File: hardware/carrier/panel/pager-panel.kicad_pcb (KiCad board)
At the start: 2 copper layers, 40 x 20 mm, 28 parts, among them J1 GDEY029T94 FPC, J2 CARRIER, J3 FL-A FPC (FL03), J4 FL-B FPC (Orient), Q5 AO3400A

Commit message: BOM: move six passives to JLC basic parts, fix connector LCSC codes (no footprint changes)
Carrier: R32 2.2M -> 1M (C26083), C14 22nF -> 100nF (C1525), R1 22.1k -> 22k (C25768),
R2 47.5k -> 47k (C25792); J1 LCSC C160407 (SM08B), J2 MPN/LCSC SM04B-SRSS-TB C160404
to match its SH footprint.
Panel: C11 4.7uF under basic code C19666, D1-D3 NSR0530 -> B5819W (C8598, SOD-123 as
already on the board), R4 2.2R gets C22939.
Board footprint fields updated to match. ERC clean on both.

Co-Authored-By: Claude Fable 5.1 <noreply@anthropic.com>
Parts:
- D1, D2, D3: value MBR0530 -> B5819W
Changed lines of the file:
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@@
 			)
 		)
-		(property "LCSC" "C1779"
+		(property "LCSC" "C19666"
 			(at 0 0 90)
 			(layer "F.Fab")
@@
 			)
 		)
-		(property "Value" "MBR0530"
+		(property "Value" "B5819W"
 			(at 0 2.1 0)
 			(layer "F.Fab")
@@
 			)
 		)
-		(property "MPN" "MBR0530"
+		(property "MPN" "B5819W"
 			(at 0 0 0)
 			(layer "F.Fab")
@@
 			)
 		)
-		(property "LCSC" "C82046"
+		(property "LCSC" "C8598"
 			(at 0 0 0)
 			(layer "F.Fab")
@@
 			)
 		)
-		(property "Value" "MBR0530"
+		(property "Value" "B5819W"
 			(at 0 2.1 0)
 			(layer "F.Fab")
@@
 			)
 		)
-		(property "MPN" "MBR0530"
+		(property "MPN" "B5819W"
 			(at 0 0 0)
 			(layer "F.Fab")
@@
 			)
 		)
-		(property "LCSC" "C82046"
+		(property "LCSC" "C8598"
 			(at 0 0 0)
 			(layer "F.Fab")
@@
 			)
 		)
-		(property "Value" "MBR0530"
+		(property "Value" "B5819W"
 			(at 0 2.1 0)
 			(layer "F.Fab")
@@
 			)
 		)
-		(property "MPN" "MBR0530"
+		(property "MPN" "B5819W"
 			(at 0 0 0)
 			(layer "F.Fab")
@@
 			)
 		)
-		(property "LCSC" "C82046"
+		(property "LCSC" "C8598"
 			(at 0 0 0)
 			(layer "F.Fab")
@@
 			)
 		)
-		(property "LCSC" ""
+		(property "LCSC" "C22939"
 			(at 0 0 90)
 			(layer "F.Fab")

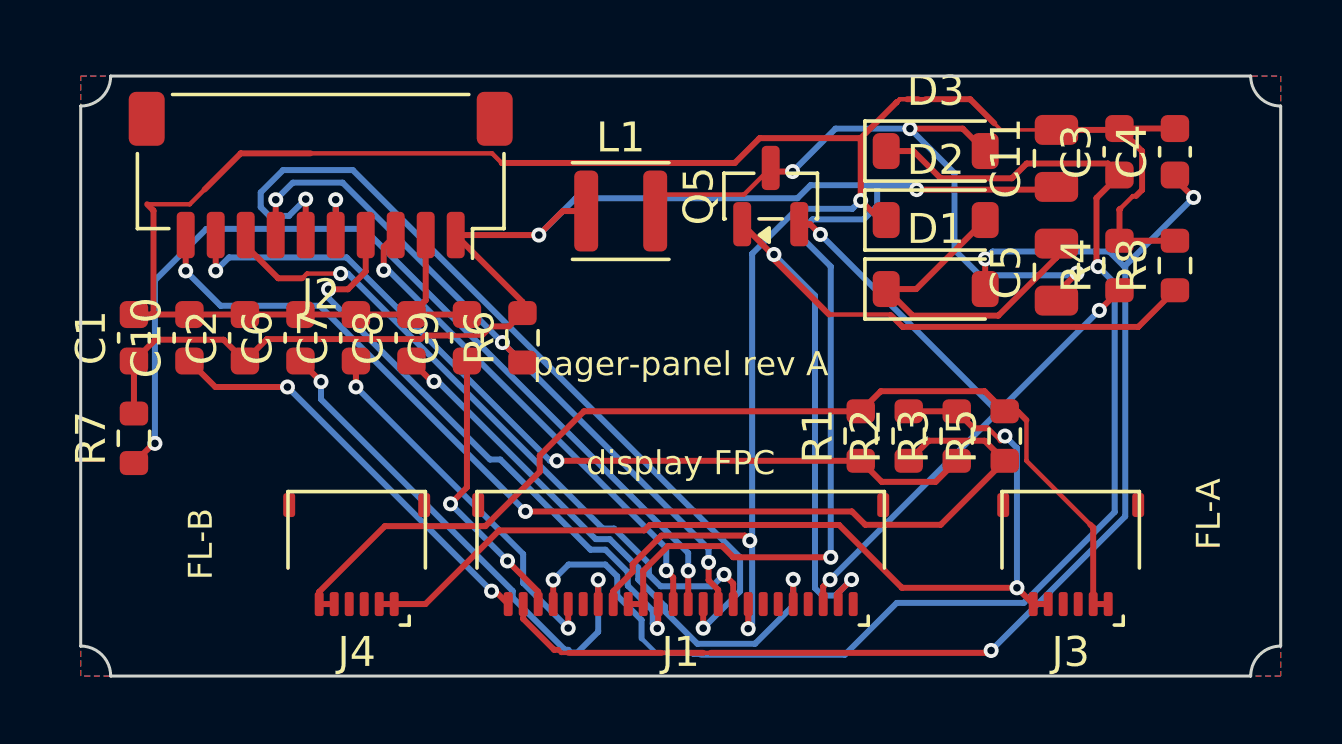
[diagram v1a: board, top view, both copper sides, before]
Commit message: Panel: split the frontlight off the carrier cable (J2 -> 8-pin SH, new J5 2-pin), re-routed
Schematic: J2 CARRIER is SM08B-SRSS-TB (C160407) on the same wires; new J5 FRONTLIGHT
SM02B-SRSS-TB (C160402) takes FL_P (pin 1) and FL_N (pin 2), matching carrier J8.
Board: J2 swapped with pins 1-8 in place, J5 at the bottom-left corner, R7 nudged,
full Freerouting pass (0 unrouted), GND pours refilled.
Known: 25 tracks below the 0.2 mm minimum width, J5 mounting pads 0.2 mm too close to
the bottom edge; owner finishing by hand.

Co-Authored-By: Claude Fable 5.1 <noreply@anthropic.com>
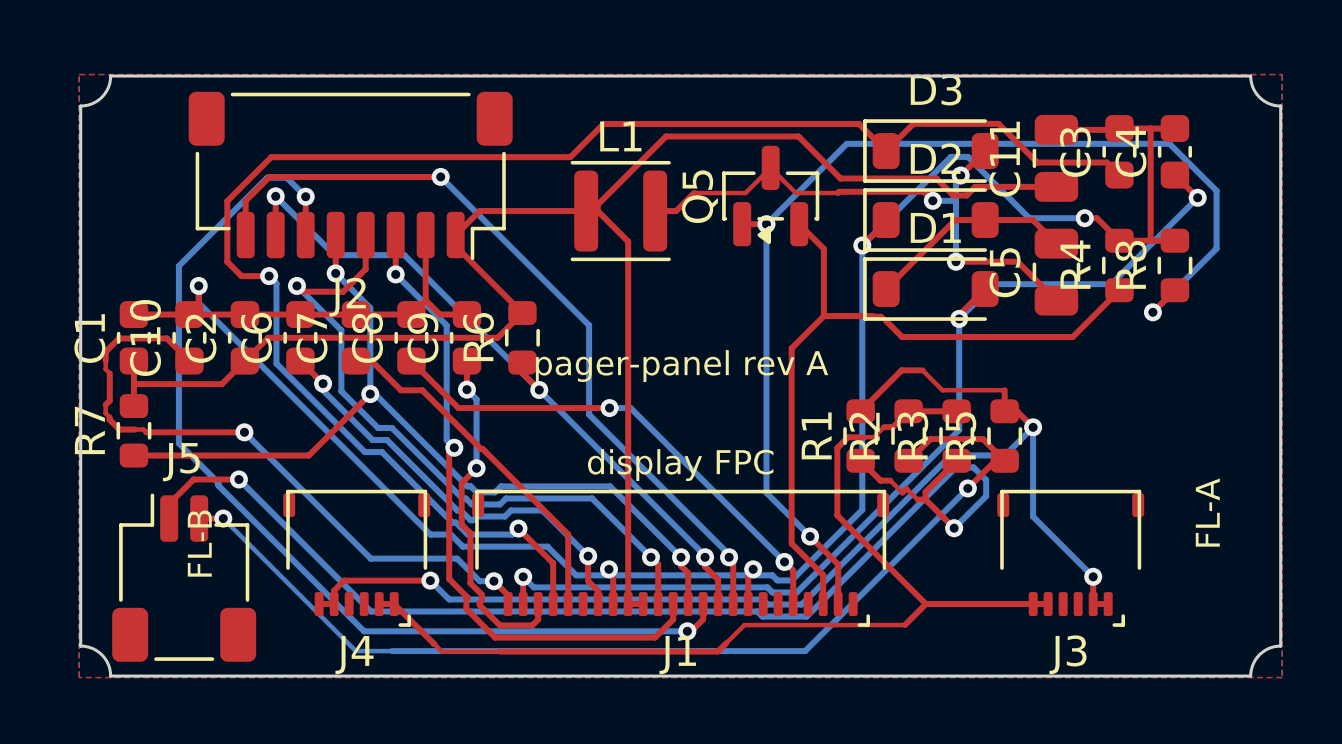
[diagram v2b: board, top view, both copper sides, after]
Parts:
- added J5: FRONTLIGHT, Connector_JST:JST_SH_SM02B-SRSS-TB_1x02-1MP_P1.00mm_Horizontal, F.Cu at (3.45, 16.8)
- J2: footprint Connector_JST:JST_SH_SM10B-SRSS-TB_1x10-1MP_P1.00mm_Horizontal -> Connector_JST:JST_SH_SM08B-SRSS-TB_1x08-1MP_P1.00mm_Horizontal
- moved J2 1.00 mm to (9.00, 3.30)
- moved R7 0.25 mm to (1.77, 11.8)
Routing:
- net GND: track 87.4 -> 75.6 mm, vias 3 -> 5
- net FL_P: track 29.5 -> 40.1 mm
- net 3V3_EPD: track 65.3 -> 55.4 mm, vias 3 -> 0
- net EPD_VGH: track 44.0 -> 52.4 mm
- net EPD_VGL: track 41.5 -> 33.6 mm
- net EPD_VCOM: track 14.0 -> 21.7 mm
- net EPD_GDR: track 30.7 -> 37.2 mm, vias 2 -> 3
- net FL_A: track 35.5 -> 41.9 mm, vias 0 -> 3
- net EINK_SCK: track 16.6 -> 21.7 mm
- net EINK_DC: track 28.9 -> 33.7 mm
- net EPD_PUMP: track 11.6 -> 6.95 mm
- net EINK_CS: track 33.2 -> 28.9 mm
- net EPD_SW: track 23.2 -> 19.1 mm
- net EINK_BUSY: track 22.6 -> 26.2 mm
- net EPD_VDD: track 17.2 -> 14.4 mm
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
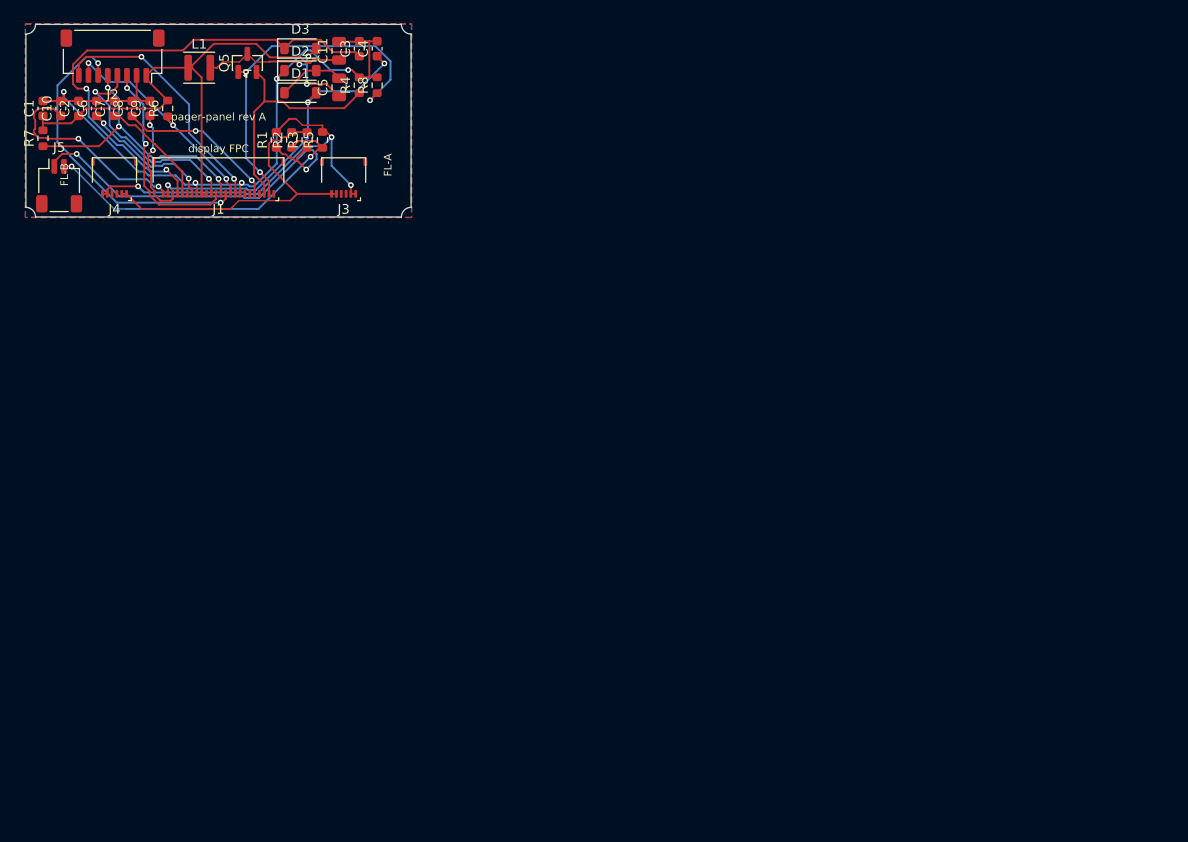
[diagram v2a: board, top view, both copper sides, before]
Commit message: Panel: solder-jumper FL polarity, front-light ZIFs at the measured tail offsets
- R1/R2/R3/R5 0R links replaced by JP1/JP2 (SolderJumper 3-pad, 1-2 bridged =
  straight, cut + bridge 2-3 = swapped); no BOM lines, zero height
- J3 (FL03) at J1.x-15.5 in the edge row, J4 (Orient) at J1.x-10.8 one row inboard,
  both on J1's pad-24 side per the Good Display and Orient drawings (the 19 Oct
  placement had FL-A on the pin-1 side)
- jumper block links only; FL_P/FL_N from J5 and the ZIF-to-jumper runs left unrouted
- owner's in-progress hand placement otherwise untouched

Co-Authored-By: Claude Fable 5.1 <noreply@anthropic.com>
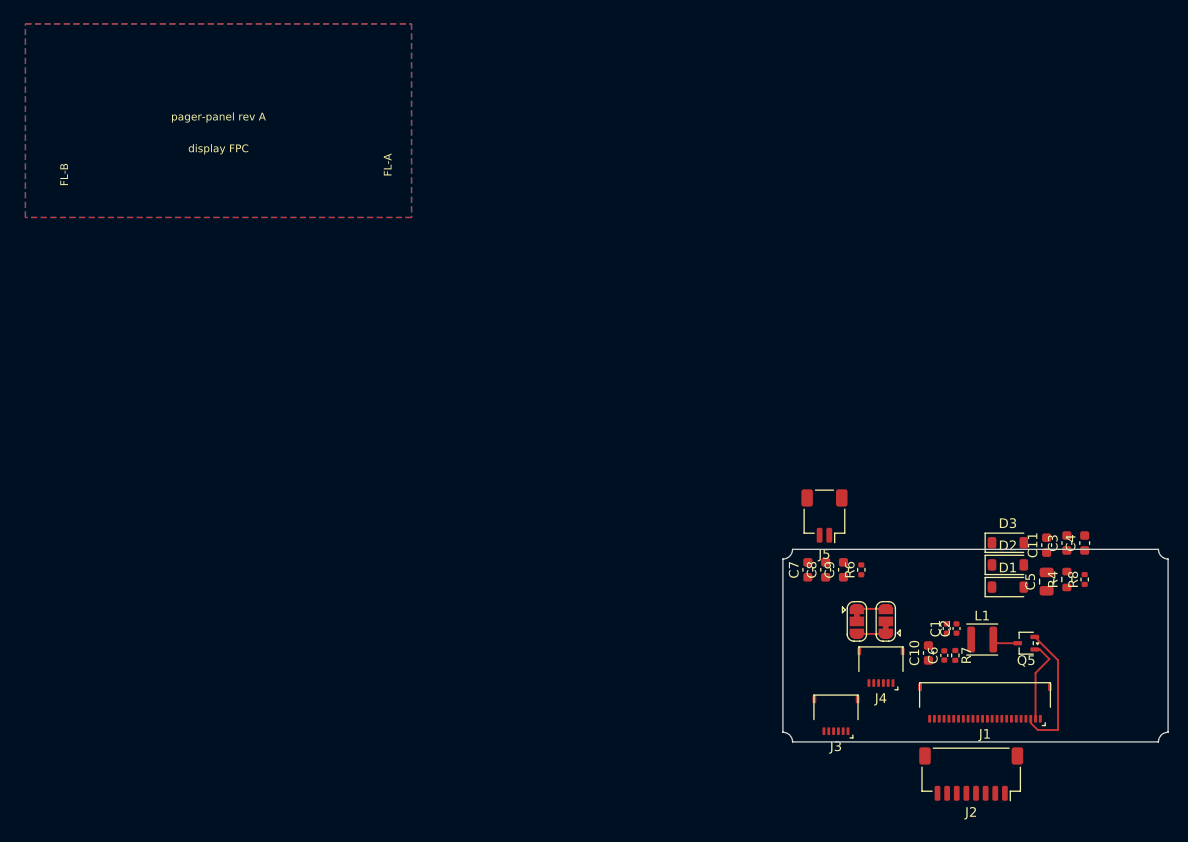
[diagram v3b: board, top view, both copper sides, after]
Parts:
- removed R1, R2, R3, R5: 0R, Resistor_SMD:R_0603_1608Metric
- added JP1: FL polarity, Jumper:SolderJumper-3_P1.3mm_Bridged12_RoundedPad1.0x1.5mm, F.Cu at (86.3, 62.0)
- added JP2: FL polarity, Jumper:SolderJumper-3_P1.3mm_Bridged12_RoundedPad1.0x1.5mm, F.Cu at (89.3, 62.0)
- C1, C2, C6: footprint Capacitor_SMD:C_0603_1608Metric -> Capacitor_SMD:C_0402_1005Metric
- C11: value 4.7uF/25V -> 4.7uF; footprint Capacitor_SMD:C_0805_2012Metric -> Capacitor_SMD:C_0603_1608Metric
- Q5: value AO3400A -> SI1308EDL; footprint Package_TO_SOT_SMD:SOT-23 -> Package_TO_SOT_SMD:SOT-323_SC-70
- R6, R7, R8: footprint Resistor_SMD:R_0603_1608Metric -> Resistor_SMD:R_0402_1005Metric
- moved J2 116.2 mm to (98.2, 77.9)
- moved R7 108.9 mm to (96.5, 65.5), turned to -90 degrees
- moved C1 108.3 mm to (95.6, 62.7)
- moved C10 106.4 mm to (93.7, 65.3)
- moved C2 106.0 mm to (96.6, 62.7)
- moved C6 104.8 mm to (95.4, 65.5)
- moved Q5 100.9 mm to (103.9, 64.3), turned to 180 degrees
- moved L1 100.7 mm to (99.3, 63.9)
- moved J1 96.5 mm to (99.6, 72.1)
- moved J4 94.4 mm to (88.8, 68.4)
- moved C11 89.6 mm to (106.0, 54.1)
- moved C3 89.6 mm to (108.1, 53.9)
- moved C4 89.6 mm to (110.0, 53.9)
- moved C5 89.6 mm to (106.0, 57.9)
- moved D1 89.6 mm to (102.0, 58.4)
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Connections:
- net EINK_BUSY renamed /panel/EINK_BUSY
- net EINK_DC renamed /panel/EINK_DC
- net EINK_MOSI renamed /panel/EINK_MOSI
- net EINK_SCK renamed /panel/EINK_SCK
- net EPD_GDR renamed /panel/EPD_GDR
- net EPD_PUMP renamed Net-(D1-K)
- net EPD_RESE renamed /panel/EPD_RESE
- net EPD_VCOM renamed /panel/EPD_VCOM
- net EPD_VDD renamed /panel/EPD_VDD
- net EPD_VGH renamed /panel/EPD_VGH
- net EPD_VGL renamed /panel/EPD_VGL
- net EPD_VSH1 renamed /panel/EPD_VSH1
- net EPD_VSH2 renamed /panel/EPD_VSH2
- net EPD_VSL renamed /panel/EPD_VSL
- J1 pad 10: EINK_RST -> /panel/EINK_RST
- J1 pad 12: EINK_CS -> /panel/EINK_CS
- J2 pad 5: EINK_CS -> /panel/EINK_CS
- J2 pad 7: EINK_RST -> /panel/EINK_RST
- R6 pad 1: EINK_RST -> 3V3_EPD
- R6 pad 2: 3V3_EPD -> /panel/EINK_RST
- R7 pad 1: EINK_CS -> 3V3_EPD
- R7 pad 2: 3V3_EPD -> /panel/EINK_CS
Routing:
- net GND: track 75.6 -> 0.00 mm, vias 5 -> 0
- net 3V3_EPD: track 55.4 -> 0.00 mm
- net /panel/EPD_VGH: track 52.4 -> 0.00 mm, vias 2 -> 0
- net FL_A: track 41.9 -> 0.00 mm, vias 3 -> 0
- net FL_P: track 40.1 -> 3.00 mm, vias 2 -> 0
- net FL_K: track 34.5 -> 0.00 mm
- net /panel/EINK_DC: track 33.7 -> 0.00 mm, vias 2 -> 0
- net /panel/EPD_VGL: track 33.6 -> 0.00 mm, vias 3 -> 0
- net FL_N: track 35.1 -> 3.00 mm, vias 2 -> 0
- net EINK_CS: track 28.9 -> 0.00 mm, vias 3 -> 0
- net /panel/EPD_GDR: track 37.2 -> 8.74 mm, vias 3 -> 0
- net /panel/EINK_BUSY: track 26.2 -> 0.00 mm, vias 2 -> 0
- net EINK_RST: track 23.5 -> 0.00 mm, vias 3 -> 0
- net /panel/EINK_MOSI: track 22.4 -> 0.00 mm, vias 2 -> 0
- net /panel/EPD_VCOM: track 21.7 -> 0.00 mm, vias 2 -> 0
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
